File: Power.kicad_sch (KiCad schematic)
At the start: 37 parts, among them U6 MP4560_QFN10, U7 LP2985-3.3, U8 LP2985-3.3, U9 MP4560_QFN10

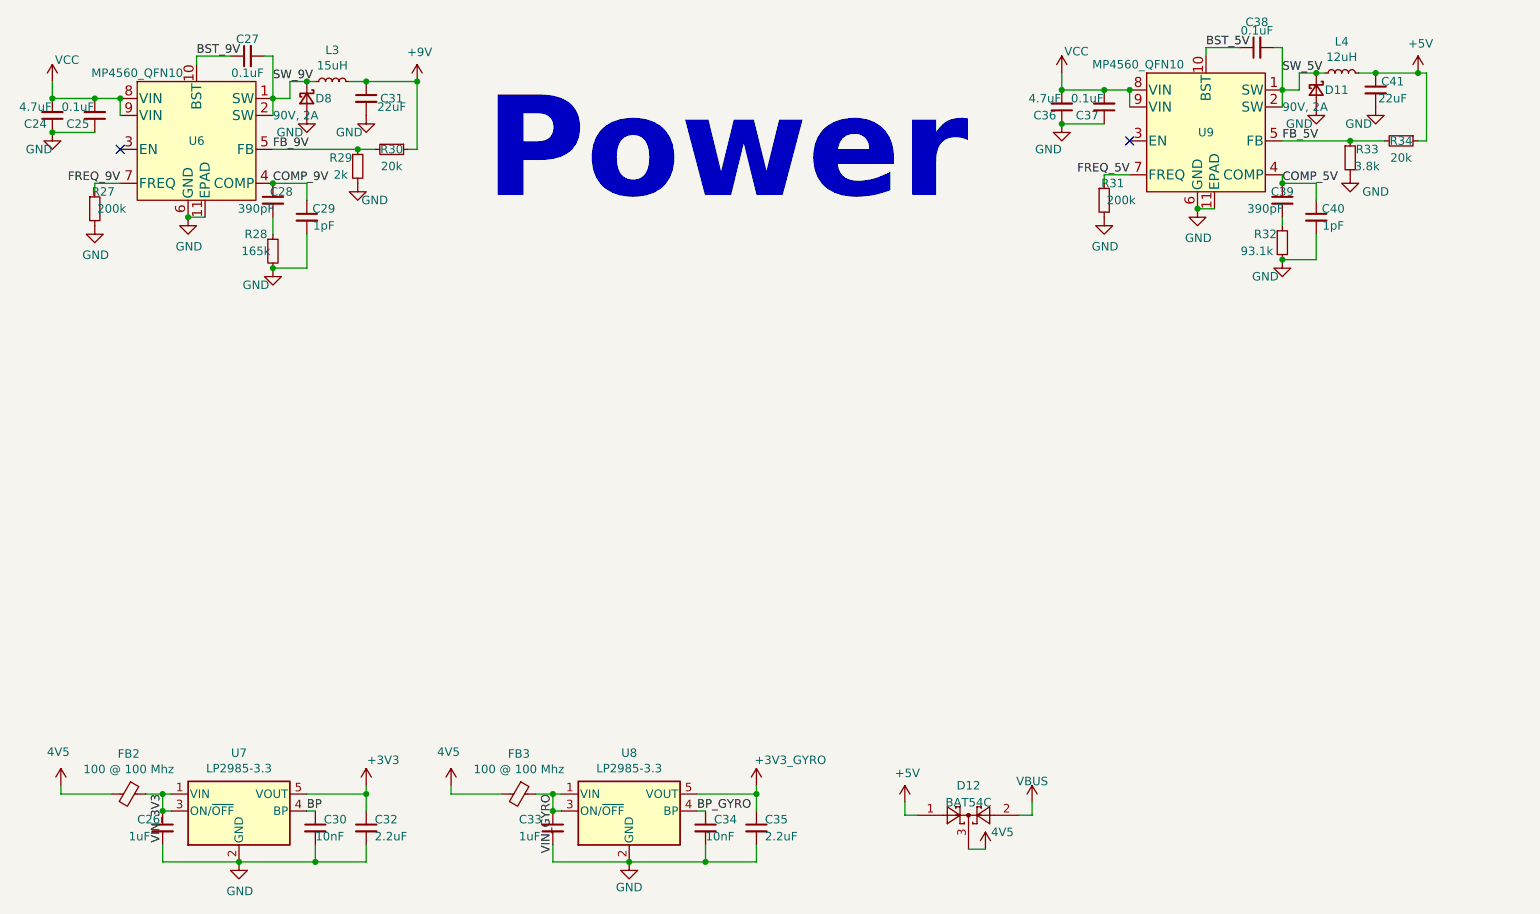
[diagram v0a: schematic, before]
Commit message: Finished power and signal routing.
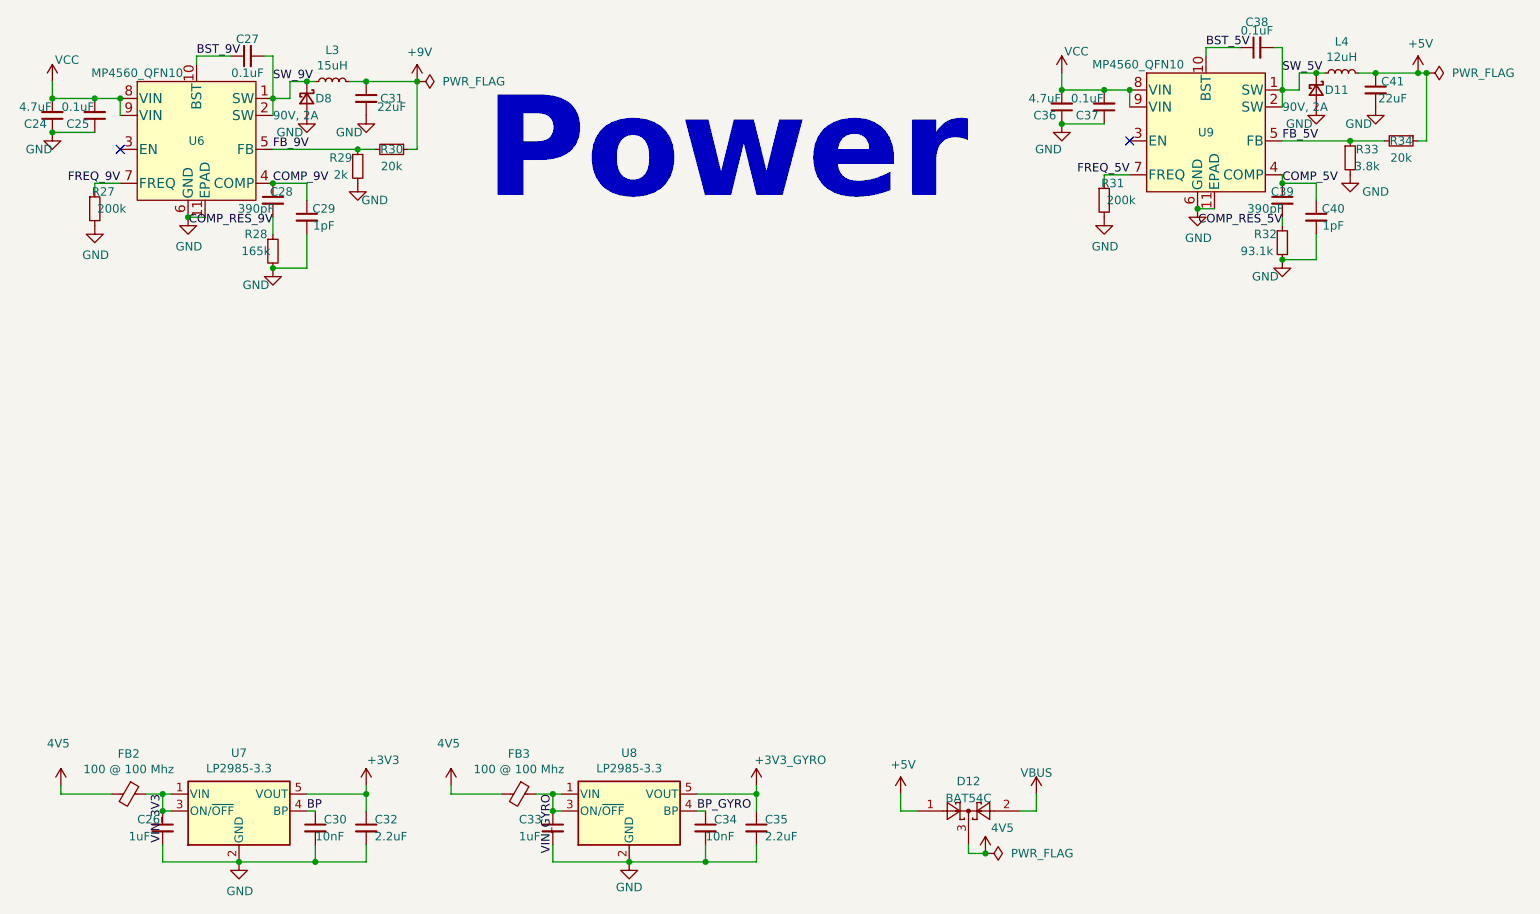
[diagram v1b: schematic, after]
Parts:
- D11, D8: footprint Diode_SMD:D_SOD-123F -> Diode_SMD:D_SOD-523
- FB2, FB3: symbol Device:Ferrite_Bead_Small -> Device:FerriteBead_Small
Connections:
- net COMP_RES_9V: now reaches C28.2, R28.1
- net COMP_RES_5V: now reaches C39.2, R32.1
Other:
- moved on the sheet: D12
